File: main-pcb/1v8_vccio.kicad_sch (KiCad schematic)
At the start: 11 parts, among them J9 CONN_DUMPTRUCK_HOST, U1 XC7S100-1FGGA484C, U29 NCP45525IMNTWG-H, U30 INA230

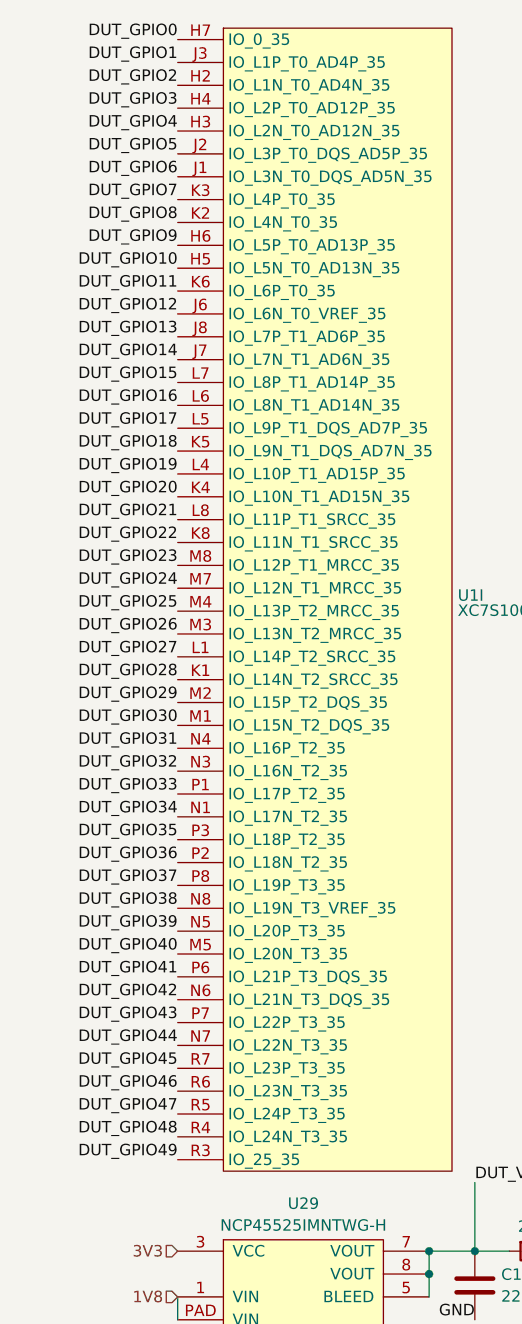
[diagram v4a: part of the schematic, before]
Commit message: First DUT socket fully routed
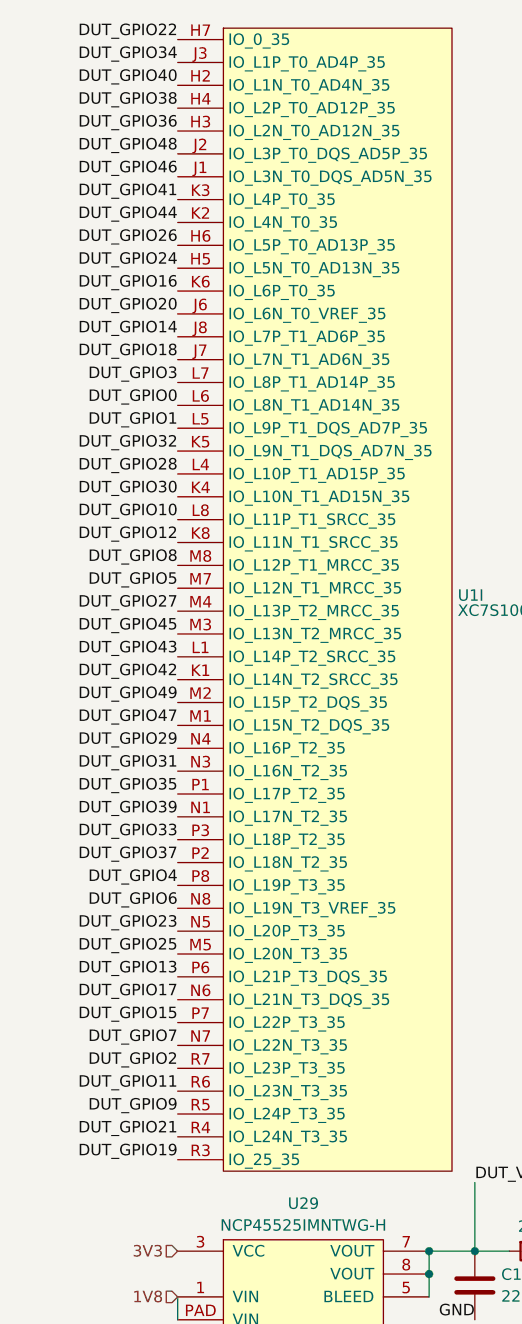
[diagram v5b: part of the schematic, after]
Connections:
- net DUT_GPIO0: now also U1.L6 (IO_L8N_T1_AD14N_35); no longer U1.H7 (IO_0_35)
- net DUT_GPIO1: now also U1.L5 (IO_L9P_T1_DQS_AD7P_35); no longer U1.J3 (IO_L1P_T0_AD4P_35)
- net DUT_GPIO10: now also U1.L8 (IO_L11P_T1_SRCC_35); no longer U1.H5 (IO_L5N_T0_AD13N_35)
- net DUT_GPIO11: now also U1.R6 (IO_L23N_T3_35); no longer U1.K6 (IO_L6P_T0_35)
- net DUT_GPIO12: now also U1.K8 (IO_L11N_T1_SRCC_35); no longer U1.J6 (IO_L6N_T0_VREF_35)
- net DUT_GPIO13: now also U1.P6 (IO_L21P_T3_DQS_35); no longer U1.J8 (IO_L7P_T1_AD6P_35)
- net DUT_GPIO14: now also U1.J8 (IO_L7P_T1_AD6P_35); no longer U1.J7 (IO_L7N_T1_AD6N_35)
- net DUT_GPIO15: now also U1.P7 (IO_L22P_T3_35); no longer U1.L7 (IO_L8P_T1_AD14P_35)
- net DUT_GPIO16: now also U1.K6 (IO_L6P_T0_35); no longer U1.L6 (IO_L8N_T1_AD14N_35)
- net DUT_GPIO17: now also U1.N6 (IO_L21N_T3_DQS_35); no longer U1.L5 (IO_L9P_T1_DQS_AD7P_35)
- net DUT_GPIO18: now also U1.J7 (IO_L7N_T1_AD6N_35); no longer U1.K5 (IO_L9N_T1_DQS_AD7N_35)
- net DUT_GPIO19: now also U1.R3 (IO_25_35); no longer U1.L4 (IO_L10P_T1_AD15P_35)
- net DUT_GPIO2: now also U1.R7 (IO_L23P_T3_35); no longer U1.H2 (IO_L1N_T0_AD4N_35)
- net DUT_GPIO20: now also U1.J6 (IO_L6N_T0_VREF_35); no longer U1.K4 (IO_L10N_T1_AD15N_35)
- net DUT_GPIO21: now also U1.R4 (IO_L24N_T3_35); no longer U1.L8 (IO_L11P_T1_SRCC_35)
- net DUT_GPIO22: now also U1.H7 (IO_0_35); no longer U1.K8 (IO_L11N_T1_SRCC_35)
- net DUT_GPIO23: now also U1.N5 (IO_L20P_T3_35); no longer U1.M8 (IO_L12P_T1_MRCC_35)
- net DUT_GPIO24: now also U1.H5 (IO_L5N_T0_AD13N_35); no longer U1.M7 (IO_L12N_T1_MRCC_35)
- net DUT_GPIO25: now also U1.M5 (IO_L20N_T3_35); no longer U1.M4 (IO_L13P_T2_MRCC_35)
- net DUT_GPIO26: now also U1.H6 (IO_L5P_T0_AD13P_35); no longer U1.M3 (IO_L13N_T2_MRCC_35)
- net DUT_GPIO27: now also U1.M4 (IO_L13P_T2_MRCC_35); no longer U1.L1 (IO_L14P_T2_SRCC_35)
- net DUT_GPIO28: now also U1.L4 (IO_L10P_T1_AD15P_35); no longer U1.K1 (IO_L14N_T2_SRCC_35)
- net DUT_GPIO29: now also U1.N4 (IO_L16P_T2_35); no longer U1.M2 (IO_L15P_T2_DQS_35)
- net DUT_GPIO3: now also U1.L7 (IO_L8P_T1_AD14P_35); no longer U1.H4 (IO_L2P_T0_AD12P_35)
- net DUT_GPIO30: now also U1.K4 (IO_L10N_T1_AD15N_35); no longer U1.M1 (IO_L15N_T2_DQS_35)
- net DUT_GPIO31: now also U1.N3 (IO_L16N_T2_35); no longer U1.N4 (IO_L16P_T2_35)
- net DUT_GPIO32: now also U1.K5 (IO_L9N_T1_DQS_AD7N_35); no longer U1.N3 (IO_L16N_T2_35)
- net DUT_GPIO33: now also U1.P3 (IO_L18P_T2_35); no longer U1.P1 (IO_L17P_T2_35)
- net DUT_GPIO34: now also U1.J3 (IO_L1P_T0_AD4P_35); no longer U1.N1 (IO_L17N_T2_35)
- net DUT_GPIO35: now also U1.P1 (IO_L17P_T2_35); no longer U1.P3 (IO_L18P_T2_35)
- net DUT_GPIO36: now also U1.H3 (IO_L2N_T0_AD12N_35); no longer U1.P2 (IO_L18N_T2_35)
- net DUT_GPIO37: now also U1.P2 (IO_L18N_T2_35); no longer U1.P8 (IO_L19P_T3_35)
- net DUT_GPIO38: now also U1.H4 (IO_L2P_T0_AD12P_35); no longer U1.N8 (IO_L19N_T3_VREF_35)
- net DUT_GPIO39: now also U1.N1 (IO_L17N_T2_35); no longer U1.N5 (IO_L20P_T3_35)
- net DUT_GPIO4: now also U1.P8 (IO_L19P_T3_35); no longer U1.H3 (IO_L2N_T0_AD12N_35)
- net DUT_GPIO40: now also U1.H2 (IO_L1N_T0_AD4N_35); no longer U1.M5 (IO_L20N_T3_35)
- net DUT_GPIO41: now also U1.K3 (IO_L4P_T0_35); no longer U1.P6 (IO_L21P_T3_DQS_35)
- net DUT_GPIO42: now also U1.K1 (IO_L14N_T2_SRCC_35); no longer U1.N6 (IO_L21N_T3_DQS_35)
- net DUT_GPIO43: now also U1.L1 (IO_L14P_T2_SRCC_35); no longer U1.P7 (IO_L22P_T3_35)
- net DUT_GPIO44: now also U1.K2 (IO_L4N_T0_35); no longer U1.N7 (IO_L22N_T3_35)
- net DUT_GPIO45: now also U1.M3 (IO_L13N_T2_MRCC_35); no longer U1.R7 (IO_L23P_T3_35)
- net DUT_GPIO46: now also U1.J1 (IO_L3N_T0_DQS_AD5N_35); no longer U1.R6 (IO_L23N_T3_35)
- net DUT_GPIO47: now also U1.M1 (IO_L15N_T2_DQS_35); no longer U1.R5 (IO_L24P_T3_35)
- net DUT_GPIO48: now also U1.J2 (IO_L3P_T0_DQS_AD5P_35); no longer U1.R4 (IO_L24N_T3_35)
- net DUT_GPIO49: now also U1.M2 (IO_L15P_T2_DQS_35); no longer U1.R3 (IO_25_35)
- net DUT_GPIO5: now also U1.M7 (IO_L12N_T1_MRCC_35); no longer U1.J2 (IO_L3P_T0_DQS_AD5P_35)
- net DUT_GPIO6: now also U1.N8 (IO_L19N_T3_VREF_35); no longer U1.J1 (IO_L3N_T0_DQS_AD5N_35)
- net DUT_GPIO7: now also U1.N7 (IO_L22N_T3_35); no longer U1.K3 (IO_L4P_T0_35)
- net DUT_GPIO8: now also U1.M8 (IO_L12P_T1_MRCC_35); no longer U1.K2 (IO_L4N_T0_35)
- net DUT_GPIO9: now also U1.R5 (IO_L24P_T3_35); no longer U1.H6 (IO_L5P_T0_AD13P_35)
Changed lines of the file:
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@@
 	(title_block
 		(title "DUMPTRUCK flash dumper")
-		(date "2024-10-17")
+		(date "2024-10-18")
 		(rev "0.1")
 		(company "Antikernel Labs")
@@
 	)
 	(label "DUT_GPIO21"
-		(at 46.99 72.39 180)
+		(at 46.99 140.97 180)
 		(fields_autoplaced yes)
 		(effects
@@
 	)
 	(label "DUT_GPIO1"
-		(at 46.99 21.59 180)
+		(at 46.99 62.23 180)
 		(fields_autoplaced yes)
 		(effects
@@
 	)
 	(label "DUT_GPIO17"
-		(at 46.99 62.23 180)
+		(at 46.99 125.73 180)
 		(fields_autoplaced yes)
 		(effects
@@
 	)
 	(label "DUT_GPIO35"
+		(at 46.99 102.87 180)
+		(fields_autoplaced yes)
+		(effects
+			(font
+				(size 1.27 1.27)
+			)
+			(justify right bottom)
+		)
+	)
+	(label "DUT_GPIO33"
 		(at 46.99 107.95 180)
 		(fields_autoplaced yes)
@@
 		)
 	)
-	(label "DUT_GPIO33"
-		(at 46.99 102.87 180)
-		(fields_autoplaced yes)
-		(effects
-			(font
-				(size 1.27 1.27)
-			)
-			(justify right bottom)
-		)
-	)
 	(label "DUT_GPIO43"
-		(at 46.99 128.27 180)
+		(at 46.99 87.63 180)
 		(fields_autoplaced yes)
 		(effects
@@
 	)
 	(label "DUT_GPIO15"
-		(at 46.99 57.15 180)
+		(at 46.99 128.27 180)
 		(fields_autoplaced yes)
 		(effects
@@
 	)
 	(label "DUT_GPIO44"
-		(at 46.99 130.81 180)
+		(at 46.99 39.37 180)
 		(fields_autoplaced yes)
 		(effects
@@
 	)
 	(label "DUT_GPIO41"
-		(at 46.99 123.19 180)
+		(at 46.99 36.83 180)
 		(fields_autoplaced yes)
 		(effects
@@
 	)
 	(label "DUT_GPIO9"
-		(at 46.99 41.91 180)
+		(at 46.99 138.43 180)
 		(fields_autoplaced yes)
 		(effects
@@
 	)
 	(label "DUT_GPIO28"
-		(at 46.99 90.17 180)
+		(at 46.99 67.31 180)
 		(fields_autoplaced yes)
 		(effects
@@
 	)
 	(label "DUT_GPIO22"
-		(at 46.99 74.93 180)
+		(at 46.99 19.05 180)
 		(fields_autoplaced yes)
 		(effects
@@
 	)
 	(label "DUT_GPIO39"
-		(at 46.99 118.11 180)
+		(at 46.99 105.41 180)
 		(fields_autoplaced yes)
 		(effects
@@
 	)
 	(label "DUT_GPIO38"
-		(at 46.99 115.57 180)
+		(at 46.99 26.67 180)
 		(fields_autoplaced yes)
 		(effects
@@
 	)
 	(label "DUT_GPIO23"
-		(at 46.99 77.47 180)
+		(at 46.99 118.11 180)
 		(fields_autoplaced yes)
 		(effects
@@
 	)
 	(label "DUT_GPIO18"
-		(at 46.99 64.77 180)
+		(at 46.99 54.61 180)
 		(fields_autoplaced yes)
 		(effects
@@
 	)
 	(label "DUT_GPIO20"
-		(at 46.99 69.85 180)
+		(at 46.99 49.53 180)
 		(fields_autoplaced yes)
 		(effects
@@
 	)
 	(label "DUT_GPIO14"
-		(at 46.99 54.61 180)
+		(at 46.99 52.07 180)
 		(fields_autoplaced yes)
 		(effects
@@
 	)
 	(label "DUT_GPIO45"
-		(at 46.99 133.35 180)
+		(at 46.99 85.09 180)
 		(fields_autoplaced yes)
 		(effects
@@
 	)
 	(label "DUT_GPIO7"
-		(at 46.99 36.83 180)
+		(at 46.99 130.81 180)
 		(fields_autoplaced yes)
 		(effects
@@
 	)
 	(label "DUT_GPIO11"
-		(at 46.99 46.99 180)
+		(at 46.99 135.89 180)
 		(fields_autoplaced yes)
 		(effects
@@
 	)
 	(label "DUT_GPIO29"
-		(at 46.99 92.71 180)
+		(at 46.99 97.79 180)
 		(fields_autoplaced yes)
 		(effects
@@
 	)
 	(label "DUT_GPIO12"
-		(at 46.99 49.53 180)
+		(at 46.99 74.93 180)
 		(fields_autoplaced yes)
 		(effects
@@
 	)
 	(label "DUT_GPIO3"
-		(at 46.99 26.67 180)
+		(at 46.99 57.15 180)
 		(fields_autoplaced yes)
 		(effects
@@
 	)
 	(label "DUT_GPIO26"
-		(at 46.99 85.09 180)
+		(at 46.99 41.91 180)
 		(fields_autoplaced yes)
 		(effects
@@
 	)
 	(label "DUT_GPIO4"
-		(at 46.99 29.21 180)
+		(at 46.99 113.03 180)
 		(fields_autoplaced yes)
 		(effects
@@
 	)
 	(label "DUT_GPIO24"
-		(at 46.99 80.01 180)
+		(at 46.99 44.45 180)
 		(fields_autoplaced yes)
 		(effects
@@
 	)
 	(label "DUT_GPIO16"
-		(at 46.99 59.69 180)
+		(at 46.99 46.99 180)
 		(fields_autoplaced yes)
 		(effects
@@
 	)
 	(label "DUT_GPIO0"
-		(at 46.99 19.05 180)
+		(at 46.99 59.69 180)
 		(fields_autoplaced yes)
 		(effects
@@
 	)
 	(label "DUT_GPIO19"
-		(at 46.99 67.31 180)
+		(at 46.99 143.51 180)
 		(fields_autoplaced yes)
 		(effects
@@
 	)
 	(label "DUT_GPIO8"
-		(at 46.99 39.37 180)
+		(at 46.99 77.47 180)
 		(fields_autoplaced yes)
 		(effects
@@
 	)
 	(label "DUT_GPIO5"
-		(at 46.99 31.75 180)
+		(at 46.99 80.01 180)
 		(fields_autoplaced yes)
 		(effects
@@
 	)
 	(label "DUT_GPIO48"
-		(at 46.99 140.97 180)
+		(at 46.99 31.75 180)
 		(fields_autoplaced yes)
 		(effects
@@
 	)
 	(label "DUT_GPIO42"
-		(at 46.99 125.73 180)
+		(at 46.99 90.17 180)
 		(fields_autoplaced yes)
 		(effects
@@
 	)
 	(label "DUT_GPIO30"
-		(at 46.99 95.25 180)
+		(at 46.99 69.85 180)
 		(fields_autoplaced yes)
 		(effects
@@
 	)
 	(label "DUT_GPIO32"
-		(at 46.99 100.33 180)
+		(at 46.99 64.77 180)
 		(fields_autoplaced yes)
 		(effects
@@
 	)
 	(label "DUT_GPIO36"
-		(at 46.99 110.49 180)
+		(at 46.99 29.21 180)
 		(fields_autoplaced yes)
 		(effects
@@
 	)
 	(label "DUT_GPIO46"
-		(at 46.99 135.89 180)
+		(at 46.99 34.29 180)
 		(fields_autoplaced yes)
 		(effects
@@
 	)
 	(label "DUT_GPIO37"
-		(at 46.99 113.03 180)
+		(at 46.99 110.49 180)
 		(fields_autoplaced yes)
 		(effects
@@
 	)
 	(label "DUT_GPIO25"
+		(at 46.99 120.65 180)
+		(fields_autoplaced yes)
+		(effects
+			(font
+				(size 1.27 1.27)
+			)
+			(justify right bottom)
+		)
+	)
+	(label "DUT_GPIO27"
 		(at 46.99 82.55 180)
 		(fields_autoplaced yes)
@@
 		)
 	)
-	(label "DUT_GPIO27"
-		(at 46.99 87.63 180)
-		(fields_autoplaced yes)
-		(effects
-			(font
-				(size 1.27 1.27)
-			)
-			(justify right bottom)
-		)
-	)
 	(label "DUT_GPIO47"
-		(at 46.99 138.43 180)
+		(at 46.99 95.25 180)
 		(fields_autoplaced yes)
 		(effects
@@
 	)
 	(label "DUT_GPIO49"
-		(at 46.99 143.51 180)
+		(at 46.99 92.71 180)
 		(fields_autoplaced yes)
 		(effects
@@
 	)
 	(label "DUT_GPIO40"
-		(at 46.99 120.65 180)
+		(at 46.99 24.13 180)
 		(fields_autoplaced yes)
 		(effects
@@
 	)
 	(label "DUT_GPIO6"
-		(at 46.99 34.29 180)
+		(at 46.99 115.57 180)
 		(fields_autoplaced yes)
 		(effects
@@
 	)
 	(label "DUT_GPIO34"
-		(at 46.99 105.41 180)
+		(at 46.99 21.59 180)
 		(fields_autoplaced yes)
 		(effects
@@
 	)
 	(label "DUT_GPIO13"
-		(at 46.99 52.07 180)
+		(at 46.99 123.19 180)
 		(fields_autoplaced yes)
 		(effects
@@
 	)
 	(label "DUT_GPIO10"
-		(at 46.99 44.45 180)
+		(at 46.99 72.39 180)
 		(fields_autoplaced yes)
 		(effects
@@
 	)
 	(label "DUT_GPIO2"
-		(at 46.99 24.13 180)
+		(at 46.99 133.35 180)
 		(fields_autoplaced yes)
 		(effects
@@
 	)
 	(label "DUT_GPIO31"
-		(at 46.99 97.79 180)
-		(fields_autoplaced yes)
-		(effects
+		(at 46.99 100.33 180)
+		(fields_autoplaced yes)
+		(effects
